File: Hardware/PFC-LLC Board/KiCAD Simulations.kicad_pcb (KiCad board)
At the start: 2 copper layers, 163.3 x 149.9 mm, 111 parts, among them J1 1792229, J2 Conn_01x02_Female, J3 1792229, J4 1792229, J5 Conn_01x02_Female, J6 1792229, Q1 C2M0160120D, U1 UCC28180DR, U1LLC1 UCC256403DDBR, U2LLC1 UCC24624DT

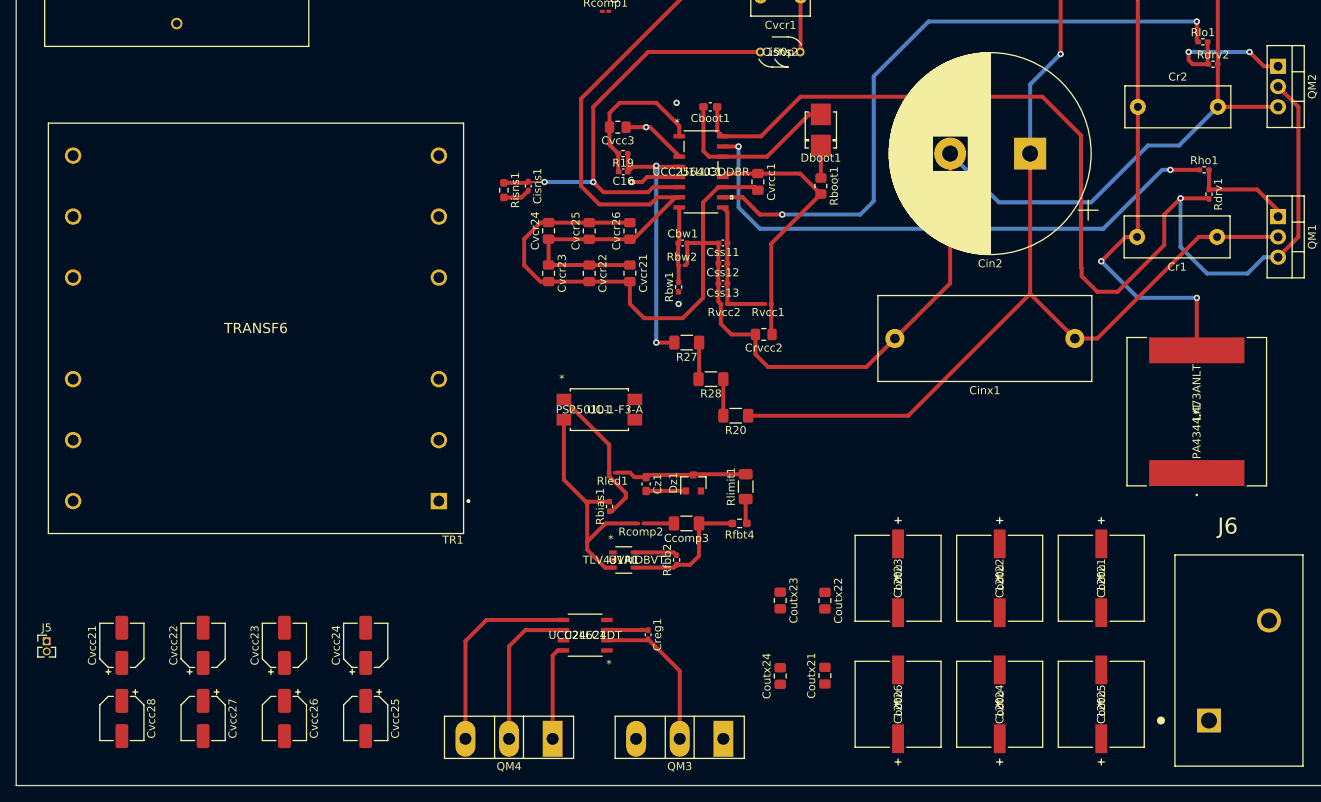
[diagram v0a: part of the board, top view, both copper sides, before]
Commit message: LLC routed (trace sizing not done)
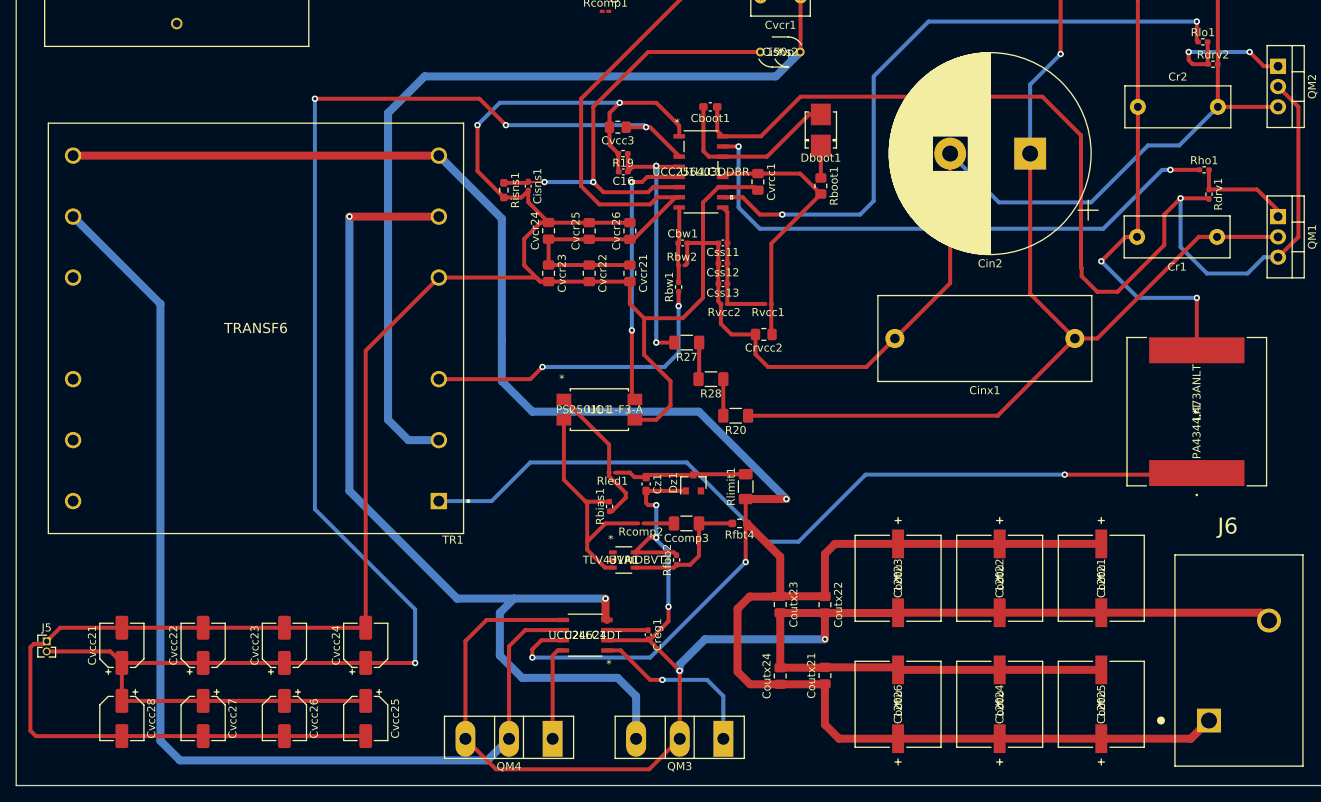
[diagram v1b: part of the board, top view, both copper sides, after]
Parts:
- moved Coutx22 0.51 mm to (151.9, 142.7)
- moved Coutx23 0.51 mm to (146.3, 142.7)
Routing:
- net Net-(Cout21-Pad1): track 3.11 -> 306.5 mm, vias 0 -> 3
- net GND: track 228.1 -> 436.0 mm, vias 0 -> 2
- net Net-(Cvcc21-Pad1): track 8.19 -> 208.7 mm, vias 1 -> 4
- net GND1: track 55.2 -> 242.3 mm, vias 0 -> 5
- net Net-(QM3-Pad3): track 0.00 -> 118.1 mm, vias 0 -> 2
- net Net-(QM4-Pad2): track 19.2 -> 135.0 mm
- net Net-(Lr1-Pad1): track 0.00 -> 104.4 mm, vias 0 -> 1
- net Net-(Cisns2-Pad2): track 105.2 -> 205.6 mm
- net Net-(Rbw1-Pad1): track 0.00 -> 39.0 mm, vias 0 -> 2
- net Net-(U1LLC1-Pad5): track 6.18 -> 33.5 mm, vias 1 -> 2
- net Net-(QM3-Pad1): track 0.00 -> 22.3 mm, vias 0 -> 1
- net Net-(Cin2-Pad1): track 137.4 -> 140.6 mm
- net (no net): vias 2 -> 0

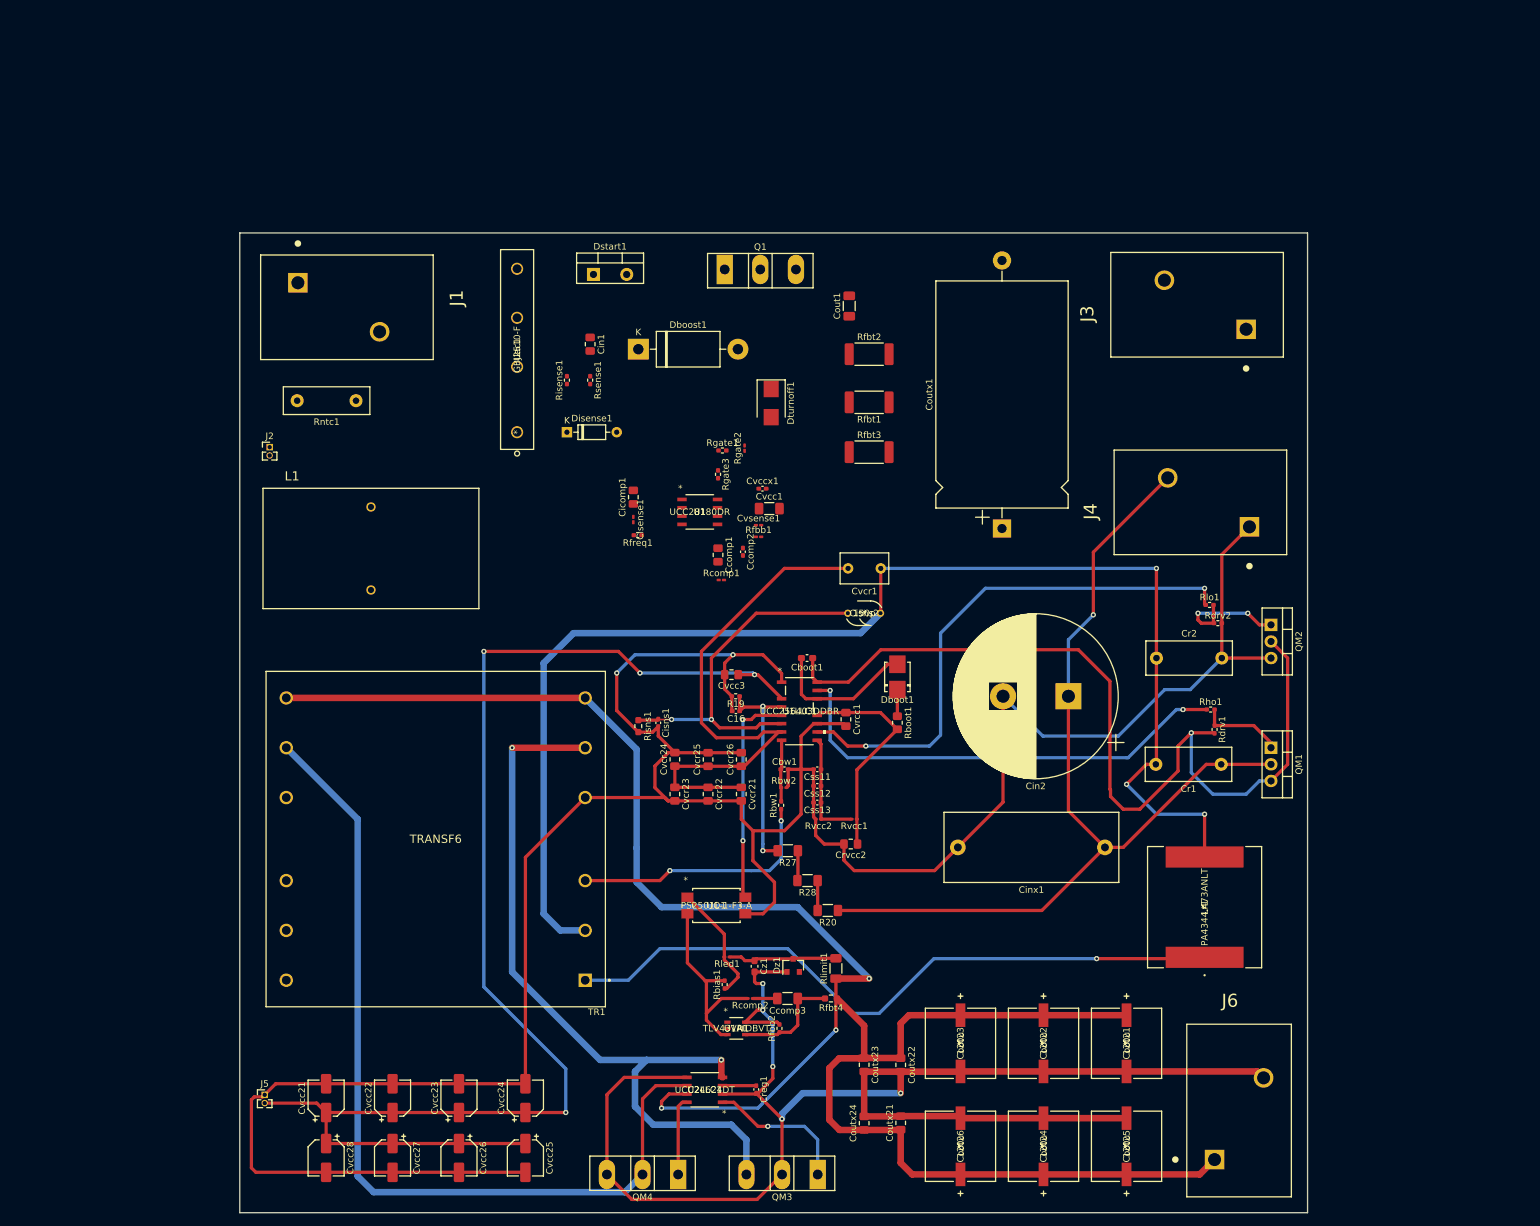
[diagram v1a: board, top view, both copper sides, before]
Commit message: Routing complete (except trace widths)
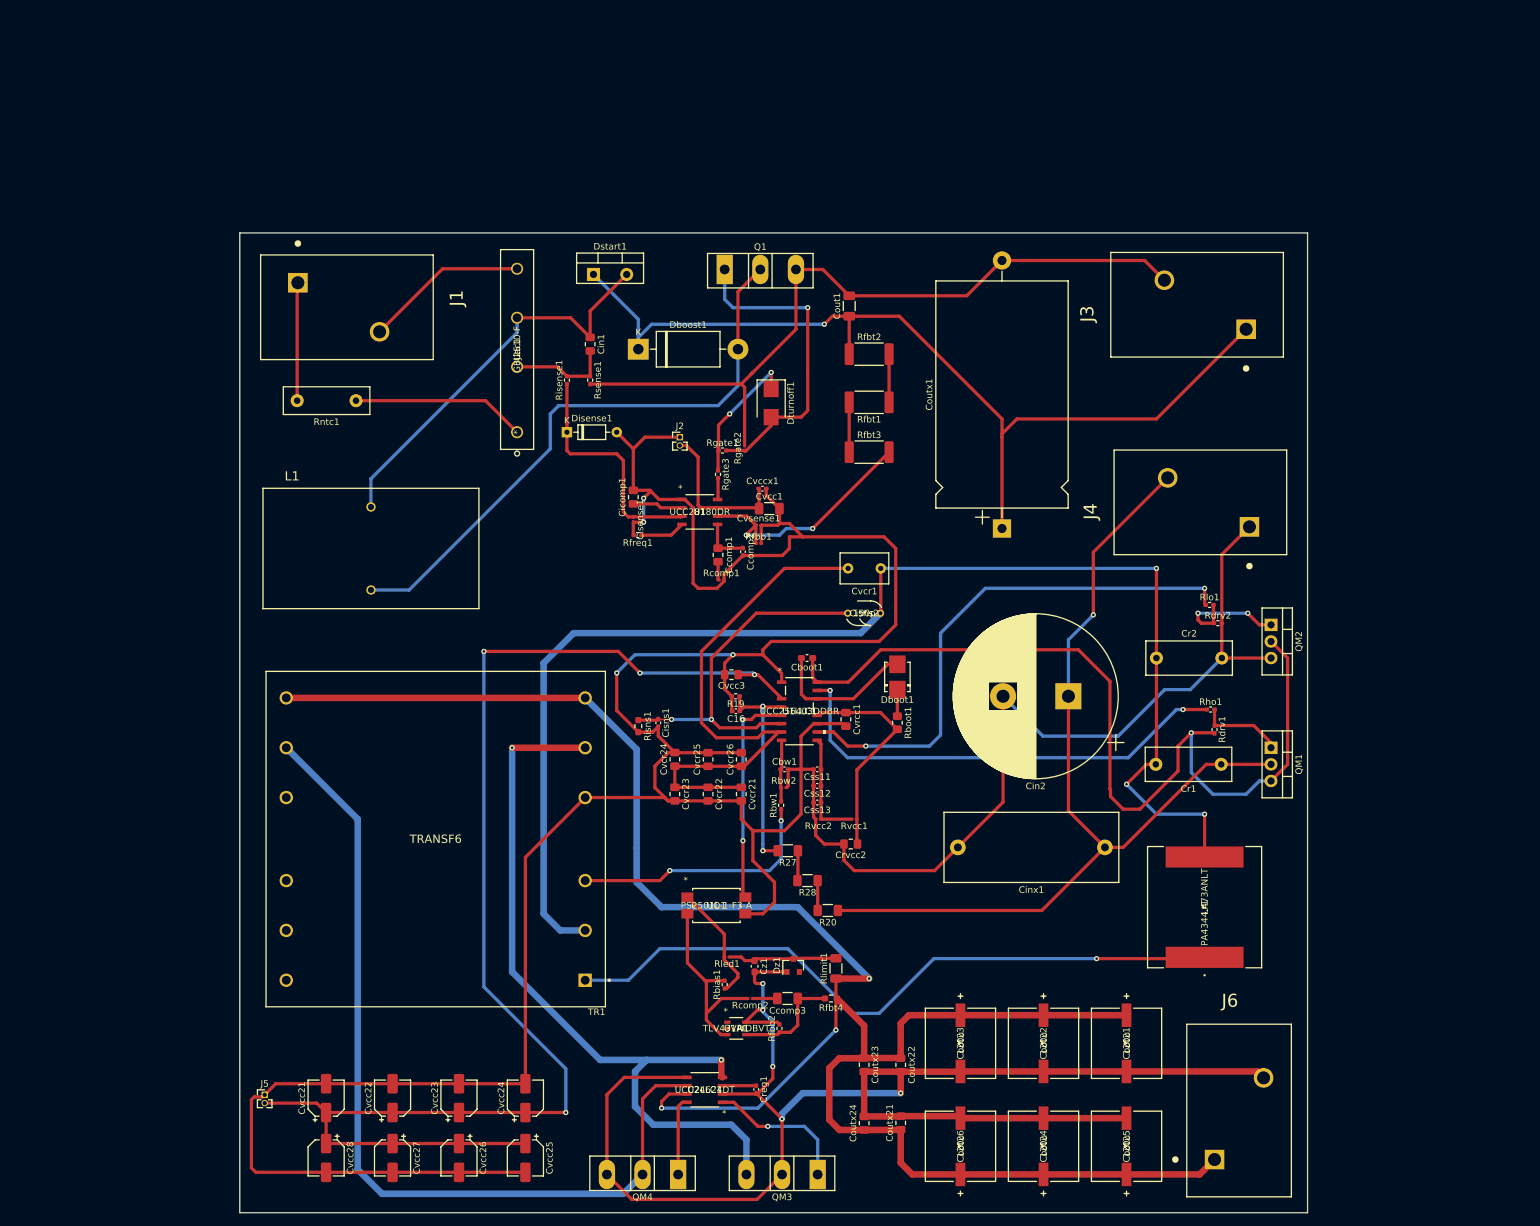
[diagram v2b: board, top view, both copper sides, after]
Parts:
- moved J2 62.8 mm to (118.1, 46.7)
- moved Rfbb1 1.02 mm to (130.1, 63.0)
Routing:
- net Net-(Cout1-Pad1): track 0.00 -> 146.1 mm, vias 0 -> 1
- net GND: track 436.0 -> 572.2 mm, vias 2 -> 4
- net Net-(Cout1-Pad2): track 0.00 -> 115.7 mm
- net Net-(Dboost1-Pad2): track 0.00 -> 91.4 mm
- net Net-(Cin1-Pad1): track 0.00 -> 62.6 mm
- net Net-(Dturnoff1-Pad2): track 0.00 -> 49.3 mm, vias 0 -> 1
- net Net-(Cvsense1-Pad1): track 0.00 -> 38.5 mm, vias 0 -> 2
- net Net-(Cisense1-Pad1): track 0.00 -> 36.6 mm
- net Net-(Rntc1-Pad1): track 0.00 -> 26.6 mm
- net Net-(J1-Pad2): track 0.00 -> 25.0 mm
- net Net-(Cvcc1-Pad1): track 0.00 -> 23.5 mm
- net Net-(Dturnoff1-Pad1): track 0.00 -> 20.9 mm, vias 0 -> 2
- net Net-(J1-Pad1): track 0.00 -> 18.1 mm
- net Net-(Cin1-Pad2): track 0.00 -> 15.6 mm
- net Net-(Cicomp1-Pad1): track 0.00 -> 7.68 mm
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
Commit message: PCB with flooding (expect GND)
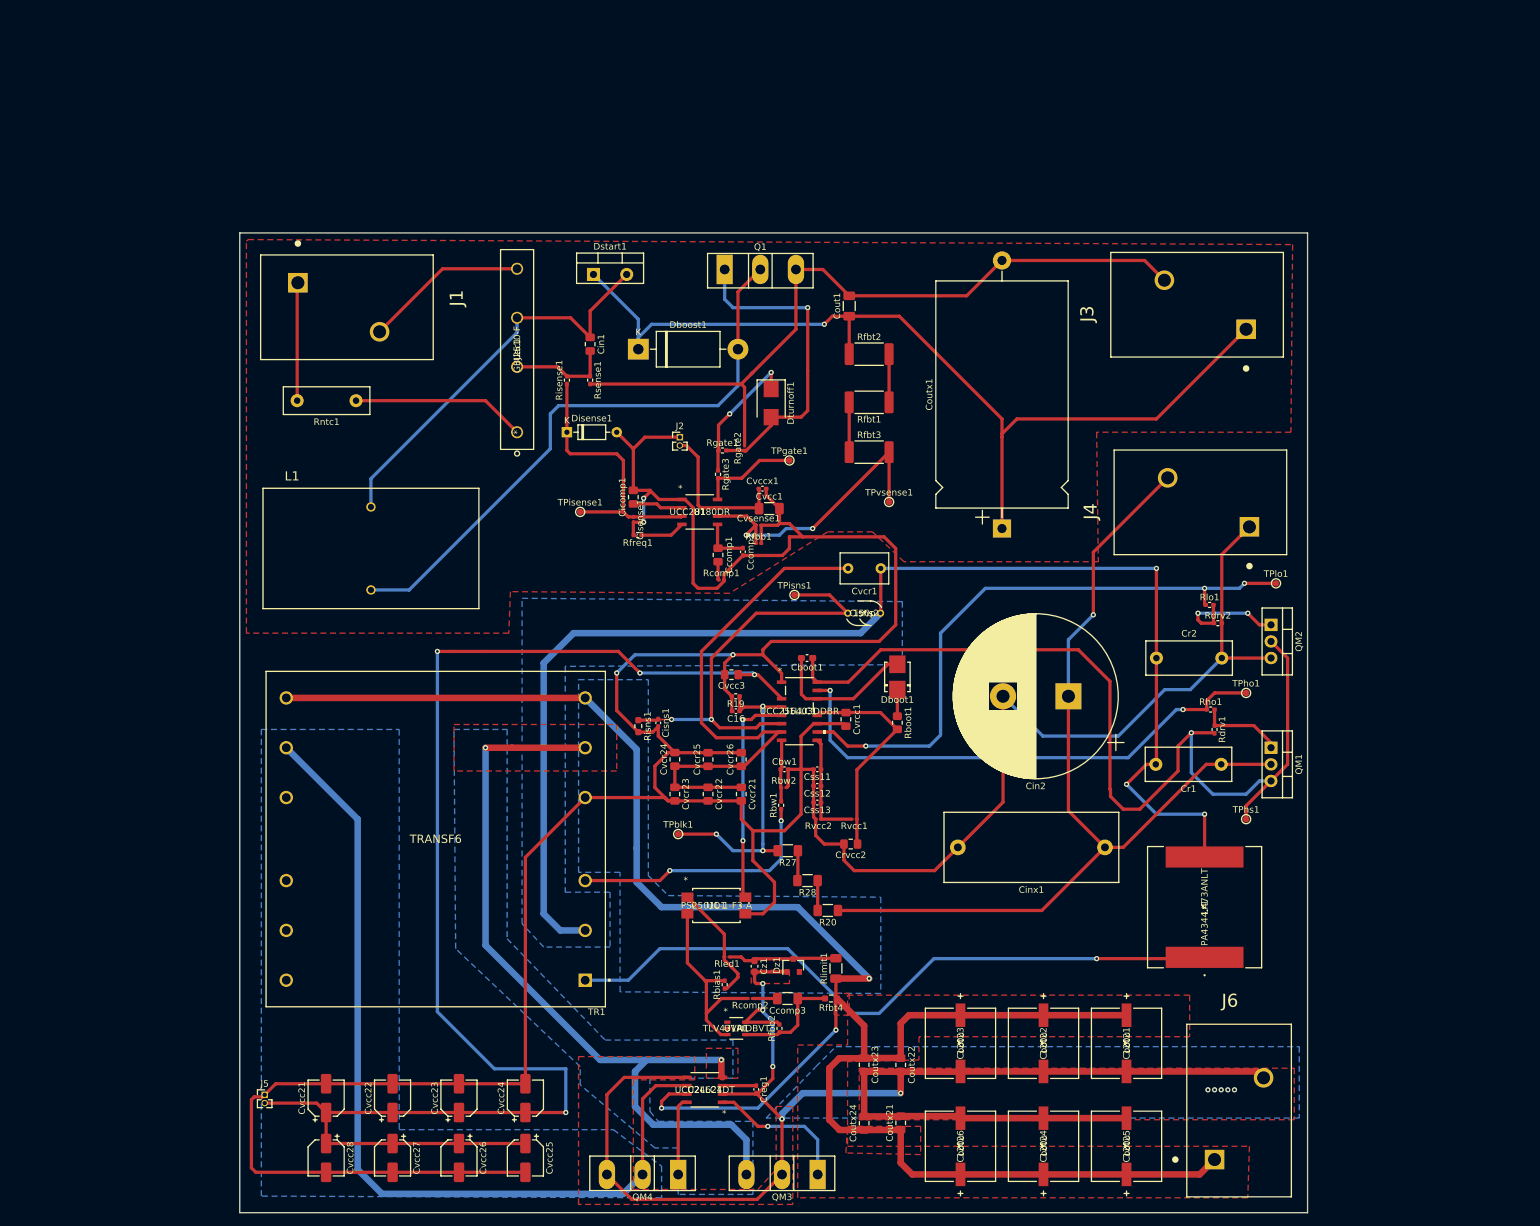
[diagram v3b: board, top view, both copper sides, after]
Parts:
- added TPblk1: TestPoint, TestPoint:TestPoint_Pad_D1.0mm, F.Cu at (117.9, 107.4)
- added TPgate1: TestPoint, TestPoint:TestPoint_Pad_D1.0mm, F.Cu at (134.9, 50.3)
- added TPho1: TestPoint, TestPoint:TestPoint_Pad_D1.0mm, F.Cu at (204.7, 85.9)
- added TPhs1: TestPoint, TestPoint:TestPoint_Pad_D1.0mm, F.Cu at (204.7, 105.2)
- added TPisense1: TestPoint, TestPoint:TestPoint_Pad_D1.0mm, F.Cu at (102.9, 58.2)
- added TPisns1: TestPoint, TestPoint:TestPoint_Pad_D1.0mm, F.Cu at (135.6, 70.9)
- added TPlo1: TestPoint, TestPoint:TestPoint_Pad_D1.0mm, F.Cu at (209.3, 69.1)
- added TPvsense1: TestPoint, TestPoint:TestPoint_Pad_D1.0mm, F.Cu at (150.1, 56.6)
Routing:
- net Net-(Cvcc21-Pad1): track 208.7 -> 225.1 mm
- net /LLC/BLK: track 33.3 -> 47.3 mm, vias 2 -> 3
- net Net-(Rgate3-Pad2): track 3.28 -> 15.3 mm
- net /LLC/LO: track 81.9 -> 93.1 mm, vias 2 -> 3
- net Net-(Cisns1-Pad1): track 55.9 -> 65.2 mm
- net /LLC/HO: track 71.4 -> 79.2 mm
- net Net-(Cvsense1-Pad1): track 38.5 -> 46.1 mm
- net /LLC/HS: track 138.2 -> 145.6 mm
- net Net-(Cisense1-Pad1): track 36.6 -> 43.2 mm
- net Net-(QM3-Pad3): track 118.1 -> 123.8 mm
- net GND1: vias 5 -> 10
- added copper zone on F.Cu, net GND
- added copper zone on B.Cu, net GND1
- added copper zone on F.Cu, net GND1
- added copper zone on B.Cu, net Net-(Cisns2-Pad2)
- added copper zone on B.Cu, net Net-(Cout21-Pad1)
- added copper zone on F.Cu, net Net-(Cout21-Pad1)
- added copper zone on B.Cu, net Net-(QM3-Pad3)
- added copper zone on F.Cu, net Net-(QM3-Pad3)
- added copper zone on B.Cu, net Net-(QM4-Pad2)

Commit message: Gerber files generated
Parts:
- Cin1: value 221.893n -> 10n
- Cout1: value 18.113m -> 13.585m
- L1: value 148.268u -> 197.691u
- moved TPhs1 6.10 mm to (198.6, 104.9)
- moved TR1 2.29 mm to (78.5, 108.2)
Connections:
- Cout1 pad 2: Net-(Cout1-Pad2) -> GND
- Coutx1 pad 2: Net-(Cout1-Pad2) -> GND
- J3 pad 2: Net-(Cout1-Pad2) -> GND
- Lr1 pad 2: Net-(Cisns2-Pad2) -> /LLC/HS
- Q1 pad 3: Net-(Cout1-Pad2) -> GND
- Rgate2 pad 2: Net-(Cout1-Pad2) -> GND
- Rsense1 pad 2: Net-(Cout1-Pad2) -> GND
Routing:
- net GND: track 572.2 -> 713.3 mm
- net Net-(Cout1-Pad2): track 115.7 -> 0.00 mm
- net Net-(Cvcc21-Pad1): track 225.1 -> 176.0 mm, vias 4 -> 2
- net Net-(Cisns2-Pad2): track 205.6 -> 160.7 mm, vias 3 -> 2
- net Net-(QM4-Pad2): track 134.6 -> 103.8 mm
- net /LLC/HS: track 145.6 -> 162.0 mm
- net Net-(QM3-Pad3): track 123.8 -> 139.2 mm, vias 2 -> 16
- net Net-(Rbw1-Pad1): track 39.0 -> 49.9 mm, vias 2 -> 1
- net Net-(Lr1-Pad1): track 104.4 -> 106.7 mm, vias 1 -> 5
- net Net-(Cout21-Pad1): track 306.5 -> 305.9 mm
- net GND1: vias 10 -> 23
- added copper zone on B.Cu, net Net-(Lr1-Pad1)
- added copper zone on F.Cu, net Net-(Lr1-Pad1)
- removed copper zone on F.Cu, net GND
- removed copper zone on B.Cu, net Net-(Cisns2-Pad2)
